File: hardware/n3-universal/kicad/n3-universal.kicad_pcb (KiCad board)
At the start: 2 copper layers, 278 x 120 mm, 131 parts, among them J1 Bornier_5.08, J10 JST-XH, J11 Bornier_5.08, J12 Bornier_5.08, J13 Support OLED, J14 Support I2C ext, J15 Header servo, J16 Header servo, J17 Header service, J18 Bornier_5.08, J19 Bornier_5.08, J2 Jack 5.5/2.1, J20 Header alim, J21 Support I2C libre, J22 Support I2C libre, J23 Bornier_5.08, J24 Bornier_5.08, J25 Bornier_5.08, J26 Bornier_5.08, J27 Bornier_5.08, J28 Support I2C libre, J29 JST-XH, J3 Bornier_5.08, J30 JST-XH, J31 Bornier_5.08, J32 Bornier_5.08, J33 Bornier_5.08, J34 Bornier_5.08, J35 Support module microSD, J36 Bornier_5.08, J37 Bornier_5.08, J4 Bornier_5.08, J5 Bornier_5.08, J6 Bornier_5.08, J7 JST-XH, J8 JST-XH, J9 JST-XH, K1 SRD-05VDC-SL-C, K2 SRD-05VDC-SL-C, K3 SRD-05VDC-SL-C, K4 SRD-05VDC-SL-C, K5 SRD-05VDC-SL-C, K6 SRD-05VDC-SL-C, Q1 BC337-40, Q10 BC337-40, Q11 NDP6020P, Q2 BC337-40, Q3 BC337-40, Q4 BC337-40, Q5 BC337-40, Q6 BC337-40, Q7 NDP6020P, Q8 BC337-40, Q9 BS250

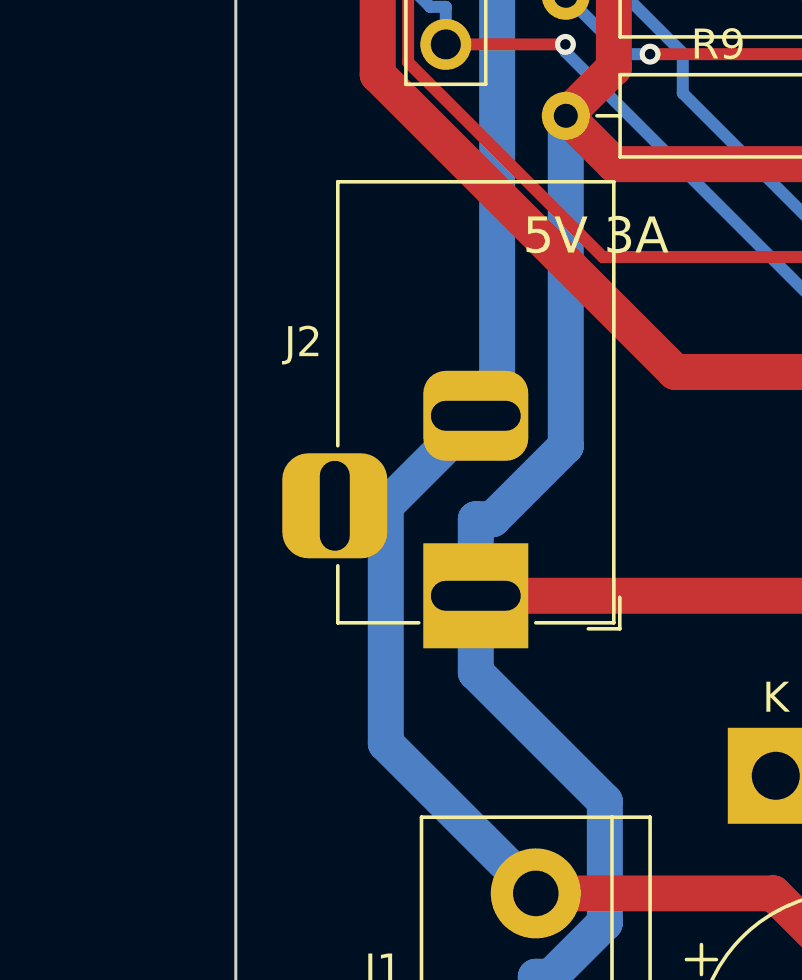
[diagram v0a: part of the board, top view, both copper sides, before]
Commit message: [n3-universal] jack J2 orienté bord gauche + tableau composants ffp5cs
L'ouverture du jack 5 V pointait vers J1 (enfichage bloqué) ; rotation 0° et couture GND, sans toucher le pad +5 V. Inventaire annoté des rôles ffp5cs sur la carte universelle.
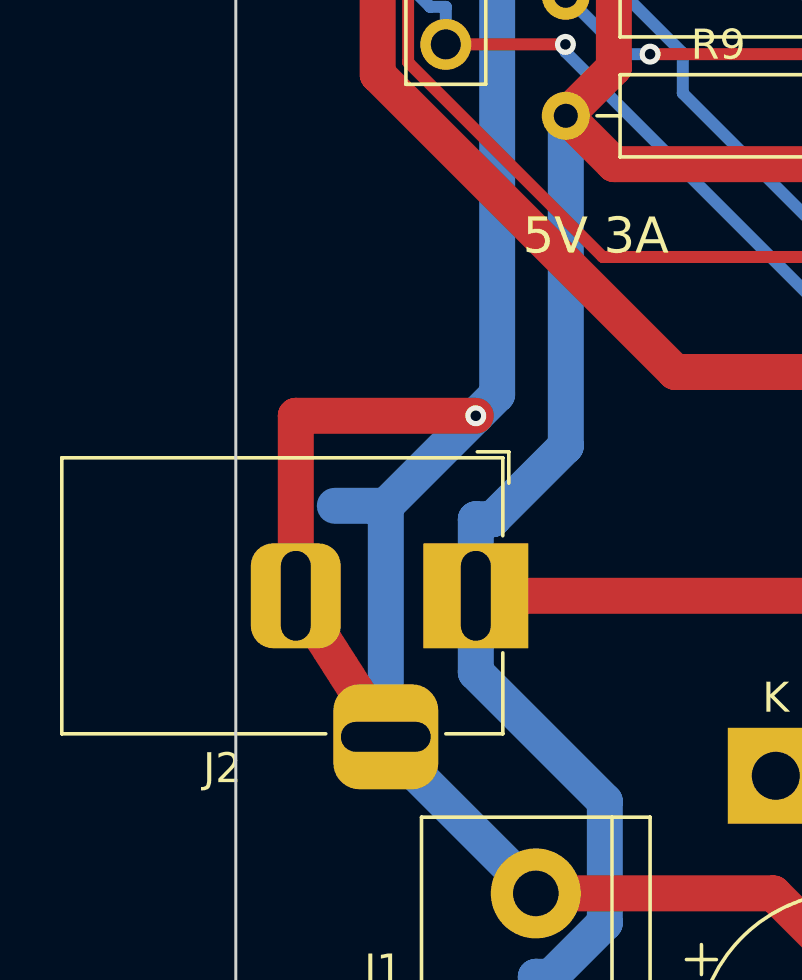
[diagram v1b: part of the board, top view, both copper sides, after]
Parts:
- turned J2 to 0 degrees
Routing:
- net GND: track 912.5 -> 930.1 mm
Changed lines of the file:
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@@
 	(footprint "n3u:BarrelJack_Horizontal"
 		(layer "F.Cu")
-		(at 48 116 -90)
+		(at 48 116)
 		(descr "DC Barrel Jack")
 		(tags "Power Jack")
@@
 		)
 		(pad "1" thru_hole rect
-			(at 0 0 270)
+			(at 0 0)
 			(size 3.5 3.5)
 			(drill oval 1 3)
@@
 		)
 		(pad "2" thru_hole roundrect
-			(at -6 0 270)
+			(at -6 0)
 			(size 3 3.5)
 			(drill oval 1 3)
@@
 		)
 		(pad "3" thru_hole roundrect
-			(at -3 4.7 270)
+			(at -3 4.7)
 			(size 3.5 3.5)
 			(drill oval 3 1)
@@
 		(net 15)
 	)
+	(segment
+		(start 42 116)
+		(end 42 110)
+		(width 1.2)
+		(layer "F.Cu")
+		(net 15)
+	)
+	(segment
+		(start 42 110)
+		(end 48 110)
+		(width 1.2)
+		(layer "F.Cu")
+		(net 15)
+	)
+	(segment
+		(start 45 120.7)
+		(end 42 116)
+		(width 1.2)
+		(layer "F.Cu")
+		(net 15)
+	)
